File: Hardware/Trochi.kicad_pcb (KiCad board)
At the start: 2 copper layers, 18.5 x 25 mm, 53 parts, among them IC1 ICM-42688-P, J1 JST-SH, J2 JST-SH, J3 JST PH, J4 Conn_01x09, J5 Conn_01x09, J6 JST-SH, J7 JST-SH, Q1 AO3400A, Q2 AO3400A, Q3 AO3400A, Q4 AO3400A, Q5 AO3400A, U1 ME6211C33M5, U3 YX-SMD5020

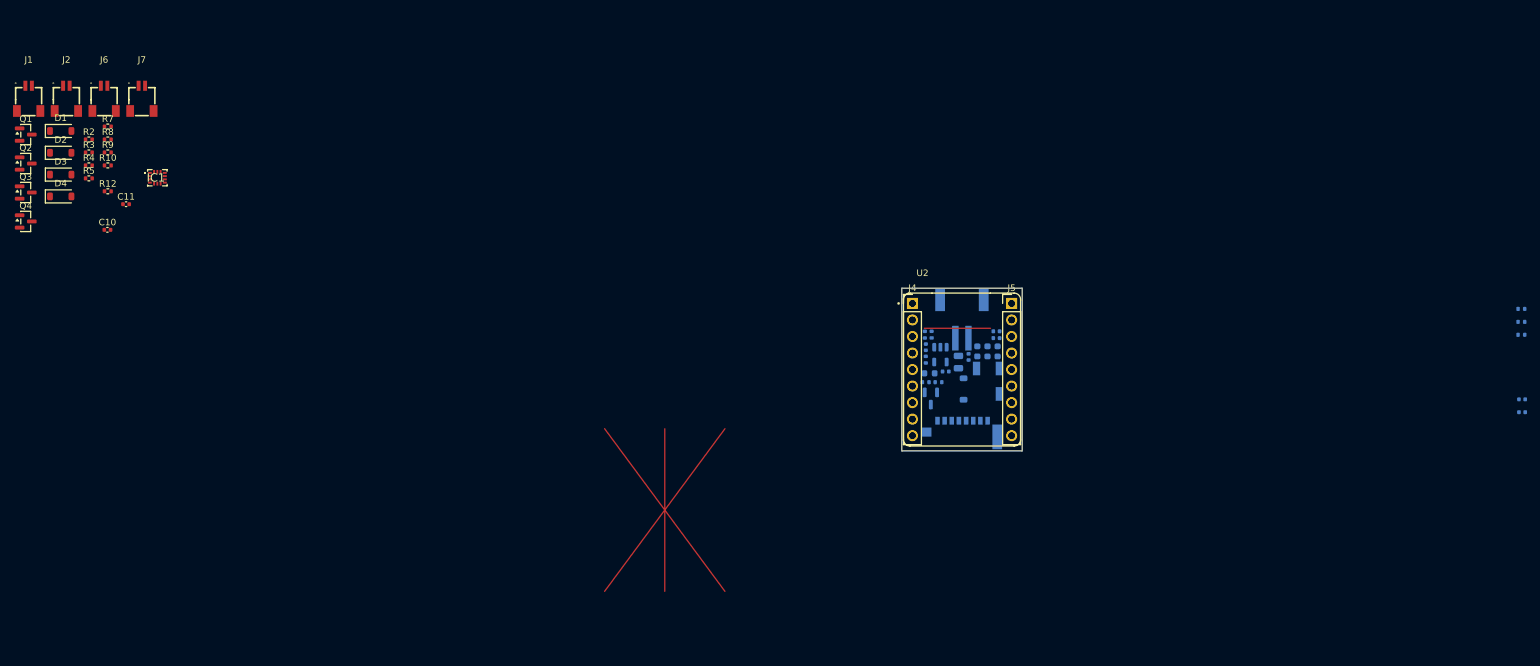
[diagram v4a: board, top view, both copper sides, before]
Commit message: feat: complete first version of bottom layer routing
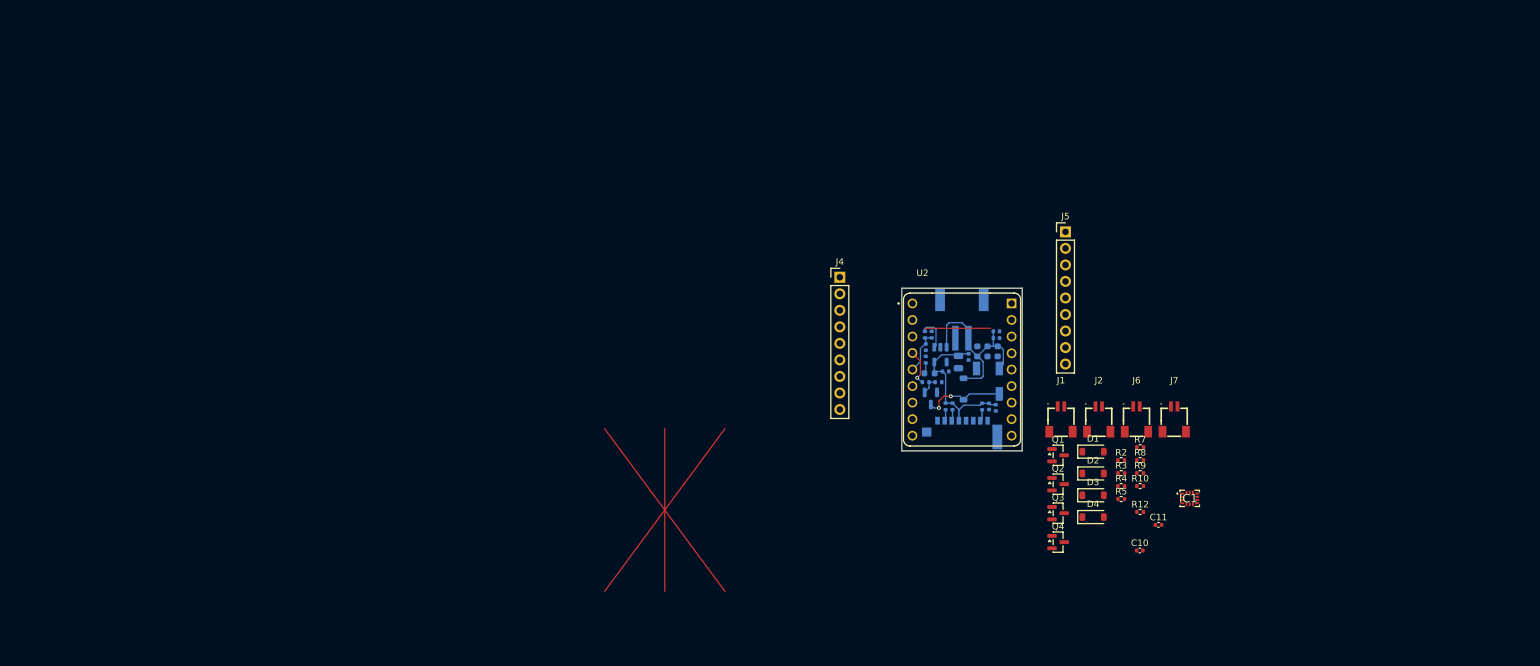
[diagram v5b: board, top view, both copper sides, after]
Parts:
- moved C10 166.1 mm to (209.1, 115.3)
- moved C11 166.1 mm to (211.9, 111.4)
- moved IC1 166.1 mm to (216.7, 107.3)
- moved J1 166.1 mm to (197.0, 95.1)
- moved J6 166.1 mm to (208.6, 95.1)
- moved J7 166.1 mm to (214.4, 95.1)
- moved R10 166.1 mm to (209.1, 105.4)
- moved R12 166.1 mm to (209.1, 109.4)
- moved R2 166.1 mm to (206.2, 101.4)
- moved R3 166.1 mm to (206.2, 103.4)
- moved R4 166.1 mm to (206.2, 105.4)
- moved R5 166.1 mm to (206.2, 107.4)
- moved R7 166.1 mm to (209.1, 99.4)
- moved R8 166.1 mm to (209.1, 101.4)
- moved R9 166.1 mm to (209.1, 103.4)
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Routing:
- net /VBAT: track 0.00 -> 34.2 mm
- net +3.3V: track 0.00 -> 24.5 mm
- net Net-(D6-A): track 0.00 -> 12.7 mm, vias 0 -> 2
- net VBAT_SENSE: track 0.00 -> 6.89 mm
- net BUZZER_CTRL: track 0.00 -> 5.58 mm, vias 0 -> 1
- net Net-(Q5-G): track 0.00 -> 2.79 mm
- net SPI_MISO: track 0.00 -> 1.78 mm
- net CS_SD: track 0.00 -> 1.74 mm
- net SPI_MOSI: track 0.00 -> 1.73 mm
- net Net-(D5-K): track 0.00 -> 1.68 mm

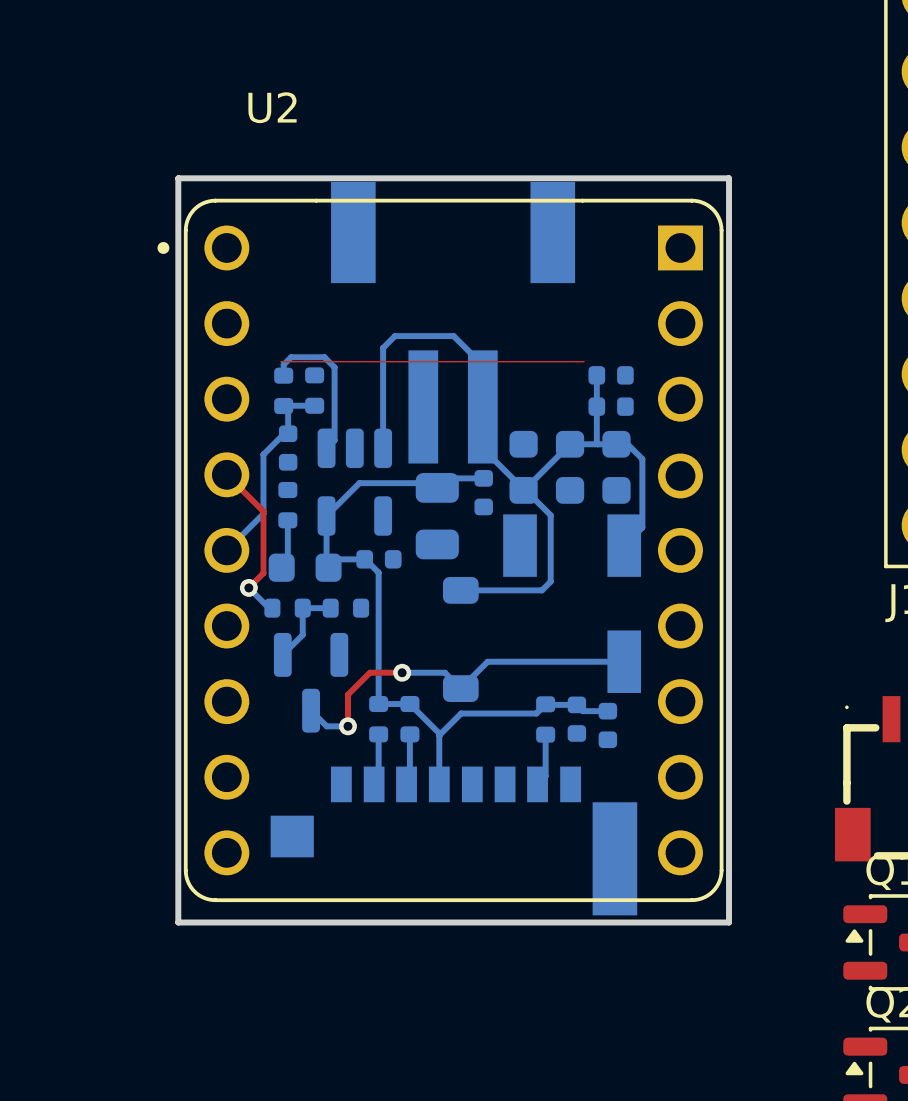
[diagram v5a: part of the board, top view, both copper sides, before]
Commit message: feat: update bottom layer routing for new SPI pinout and add ground pour
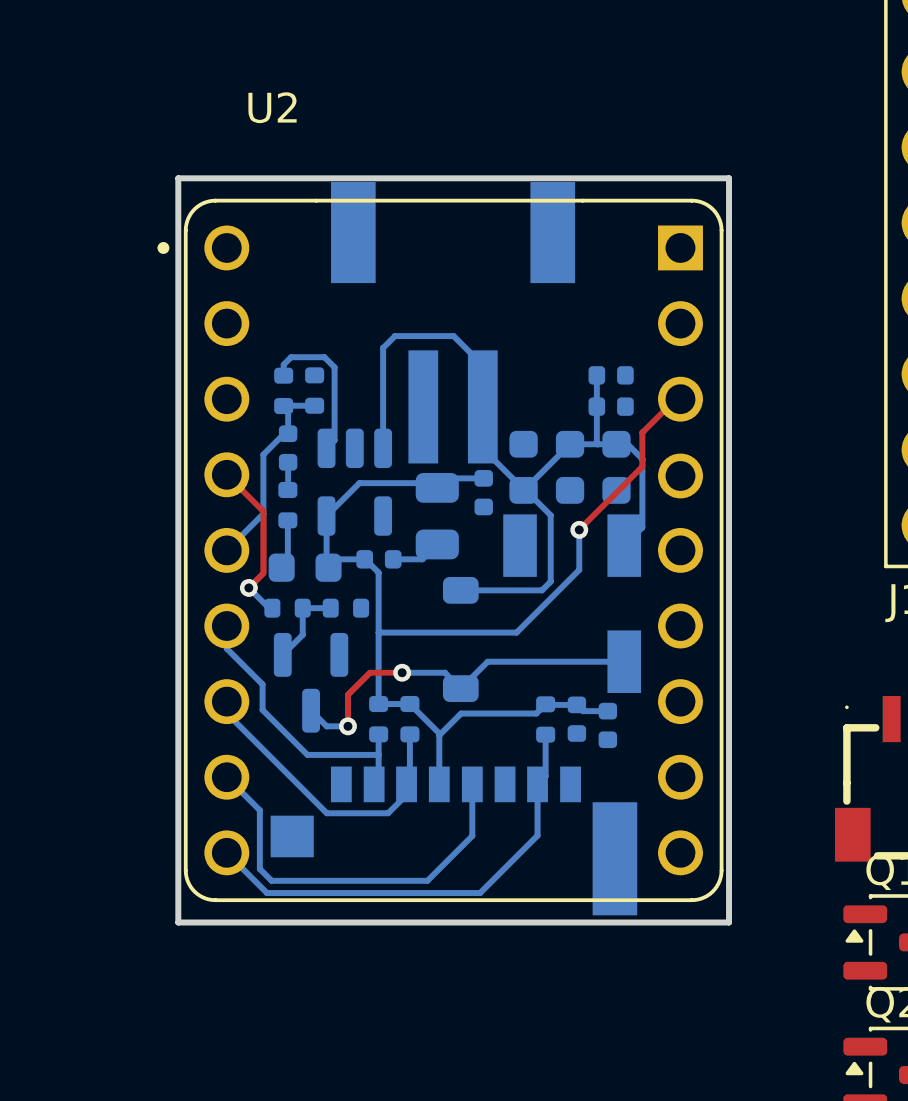
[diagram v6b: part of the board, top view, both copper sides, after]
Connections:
- U2 pad 4: SPI_MOSI -> CS_SD
- U2 pad 5: SPI_SCK -> SPI_MOSI
- U2 pad 6: SPI_MISO -> SPI_SCK
- U2 pad 7: CS_IMU -> SPI_MISO
- U2 pad 8: CS_SD -> CS_IMU
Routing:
- net +3.3V: track 24.5 -> 39.3 mm, vias 0 -> 1
- net SPI_MISO: track 1.78 -> 15.3 mm
- net SPI_SCK: track 0.00 -> 13.2 mm
- net SPI_MOSI: track 1.73 -> 10.2 mm
- net CS_SD: track 1.74 -> 9.59 mm
- net GND: track 0.01 -> 2.63 mm
- added copper zone on B.Cu, net GND

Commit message: fix: final ground pour corrections before top layer routing
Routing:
- net GND: track 2.63 -> 9.40 mm
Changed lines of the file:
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@@
+	)
+	(segment
+		(start 180.73 84.2)
+		(end 179.8975 85.0325)
+		(width 0.15)
+		(layer "B.Cu")
+		(net "GND")
 	)
 	(segment
@@
 	)
 	(segment
+		(start 180.73 82.68)
+		(end 180.73 84.2)
+		(width 0.2)
+		(layer "B.Cu")
+		(net "GND")
+	)
+	(segment
+		(start 178.43 84.64)
+		(end 178.43 84.07)
+		(width 0.2)
+		(layer "B.Cu")
+		(net "GND")
+	)
+	(segment
 		(start 176.19 84.54)
 		(end 176.19 85.46)
@@
 	)
 	(segment
+		(start 179.8975 85.0325)
+		(end 178.8225 85.0325)
+		(width 0.15)
+		(layer "B.Cu")
+		(net "GND")
+	)
+	(segment
 		(start 176.19 85.46)
 		(end 176.18 85.47)
+		(width 0.2)
+		(layer "B.Cu")
+		(net "GND")
+	)
+	(segment
+		(start 178.8225 85.0325)
+		(end 178.43 84.64)
+		(width 0.15)
+		(layer "B.Cu")
+		(net "GND")
+	)
+	(segment
+		(start 178.64 90.28)
+		(end 177.91 91.01)
+		(width 0.2)
+		(layer "B.Cu")
+		(net "GND")
+	)
+	(segment
+		(start 178.64 89.44)
+		(end 178.64 90.28)
 		(width 0.2)
 		(layer "B.Cu")
@@
 	)
 	(segment
+		(start 178.4425 85.3825)
+		(end 181.1825 85.3825)
+		(width 0.15)
+		(layer "B.Cu")
+		(net "+3.3V")
+	)
+	(segment
 		(start 181.275 93.655)
 		(end 180.28 92.66)
@@
 	)
 	(segment
-		(start 181.04 85.24)
-		(end 181.2 85.4)
-		(width 0.2)
-		(layer "B.Cu")
-		(net "+3.3V")
-	)
-	(segment
 		(start 180.28 92.66)
 		(end 179.23 92.66)
@@
 	)
 	(segment
+		(start 181.11 85.41)
+		(end 181.16 85.36)
+		(width 0.15)
+		(layer "B.Cu")
+		(net "+3.3V")
+	)
+	(segment
+		(start 181.16 85.36)
+		(end 181.2 85.4)
+		(width 0.2)
+		(layer "B.Cu")
+		(net "+3.3V")
+	)
+	(segment
 		(start 177.48 86.345)
 		(end 177.48 88.0125)
@@
 	)
 	(segment
+		(start 181.1825 85.3825)
+		(end 181.2 85.4)
+		(width 0.2)
+		(layer "B.Cu")
+		(net "+3.3V")
+	)
+	(segment
 		(start 181.52 85.08)
 		(end 181.2 85.4)
@@
 	)
 	(segment
-		(start 177.48 86.345)
-		(end 178.585 85.24)
-		(width 0.2)
-		(layer "B.Cu")
-		(net "+3.3V")
-	)
-	(segment
 		(start 179.23 88.246134)
 		(end 178.783866 87.8)
@@
 	)
 	(segment
-		(start 178.585 85.24)
-		(end 181.04 85.24)
-		(width 0.2)
+		(start 177.48 86.345)
+		(end 178.4425 85.3825)
+		(width 0.15)
 		(layer "B.Cu")
 		(net "+3.3V")
@@
 		(hatch edge 0.5)
 		(connect_pads
-			(clearance 0.5)
+			(clearance 0.3)
 		)
 		(min_thickness 0.25)

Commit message: feat: complete top layer component placement
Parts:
- removed J4, J5: Conn_01x09, Connector_PinHeader_2.54mm:PinHeader_1x09_P2.54mm_Vertical
- moved IC1 74.7 mm to (142.0, 105.9), turned to 180 degrees
- moved C11 73.9 mm to (138.2, 105.6), turned to -90 degrees
- moved C10 70.5 mm to (139.2, 105.6), turned to -90 degrees
- moved J6 70.1 mm to (138.5, 96.3), turned to 180 degrees
- moved R9 69.8 mm to (139.4, 100.8), turned to -90 degrees
- moved J7 69.3 mm to (145.1, 96.3), turned to 180 degrees
- moved R7 68.0 mm to (141.2, 102.3)
- moved R12 67.6 mm to (141.5, 108.9), turned to 90 degrees
- moved R2 66.5 mm to (140.8, 113.1), turned to 180 degrees
- moved R4 65.8 mm to (140.8, 112.1)
- moved D1 65.7 mm to (136.5, 107.1), turned to -90 degrees
- moved R10 65.0 mm to (144.2, 102.2), turned to 180 degrees
- moved D3 64.2 mm to (137.8, 103.4), turned to 180 degrees
- moved R5 63.5 mm to (143.0, 113.1), turned to 180 degrees
- moved R8 63.0 mm to (146.2, 102.7), turned to 180 degrees
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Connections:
- U2 pad 10: PWM_M1 -> CS_IMU
- U2 pad 11: PWM_M2 -> IMU_INT
- U2 pad 8: CS_IMU -> PWM_M1
- U2 pad 9: IMU_INT -> PWM_M2
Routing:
- net Net-(D6-A): track 12.7 -> 11.6 mm
